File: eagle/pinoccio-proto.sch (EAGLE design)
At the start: 3 parts

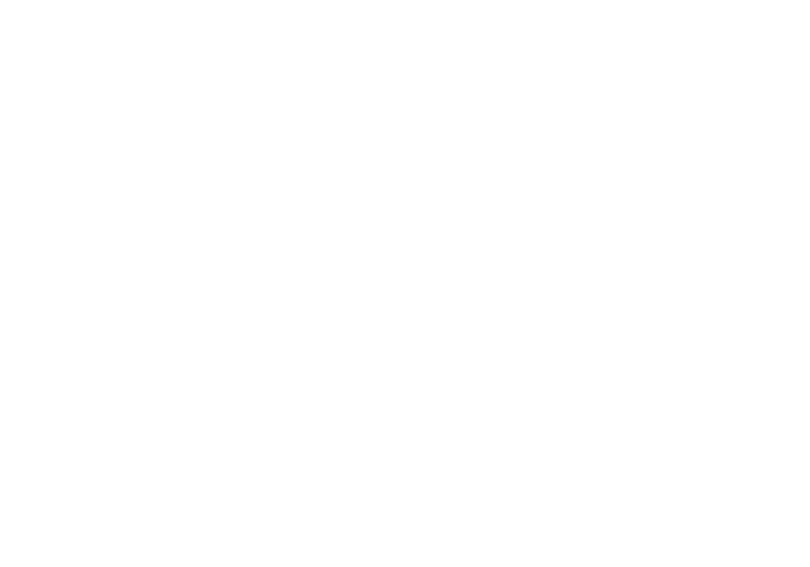
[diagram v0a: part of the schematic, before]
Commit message: Break out ground and power buses to pins
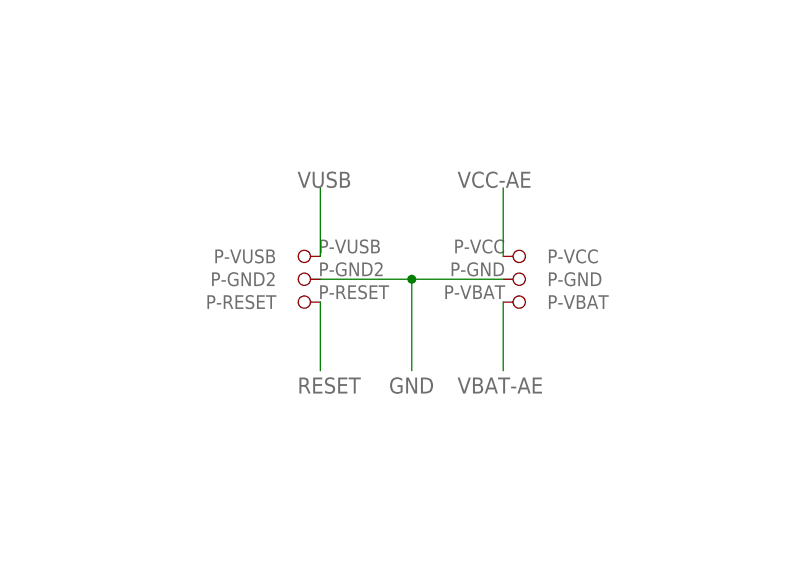
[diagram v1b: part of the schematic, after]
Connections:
- net GND: now also U$1.P$53, U$1.P$77, U$1.P-GND, U$1.P-GND2
- net RESET: now also U$1.P-RESET
- net VBAT-AE: now also U$1.P-VBAT
- net VCC-AE: now also U$1.P-VCC
- net VUSB: now also U$1.P-VUSB
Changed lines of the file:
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@@
 <label x="185.42" y="119.38" size="1.778" layer="95"/>
+</segment>
+<segment>
+<pinref part="U$1" gate="G$1" pin="P-GND"/>
+<pinref part="U$1" gate="G$1" pin="P-GND2"/>
+<wire x1="116.84" y1="127" x2="106.68" y2="127" width="0.1524" layer="91"/>
+<pinref part="U$1" gate="G$1" pin="P$77"/>
+<wire x1="96.52" y1="127" x2="106.68" y2="127" width="0.1524" layer="91"/>
+<pinref part="U$1" gate="G$1" pin="P$53"/>
+<wire x1="106.68" y1="127" x2="106.68" y2="116.84" width="0.1524" layer="91"/>
+<junction x="106.68" y="127"/>
+<label x="104.14" y="114.3" size="1.778" layer="95"/>
 </segment>
 </net>
@@
 <label x="185.42" y="175.26" size="1.778" layer="95"/>
 </segment>
+<segment>
+<pinref part="U$1" gate="G$1" pin="P-VUSB"/>
+<wire x1="96.52" y1="129.54" x2="96.52" y2="137.16" width="0.1524" layer="91"/>
+<label x="93.98" y="137.16" size="1.778" layer="95"/>
+</segment>
 </net>
 <net name="VBAT-AE" class="0">
@@
 <label x="185.42" y="116.84" size="1.778" layer="95"/>
 </segment>
+<segment>
+<pinref part="U$1" gate="G$1" pin="P-VBAT"/>
+<wire x1="116.84" y1="124.46" x2="116.84" y2="116.84" width="0.1524" layer="91"/>
+<label x="111.76" y="114.3" size="1.778" layer="95"/>
+</segment>
 </net>
 <net name="SSN" class="0">
@@
 <label x="185.42" y="170.18" size="1.778" layer="95"/>
 </segment>
+<segment>
+<pinref part="U$1" gate="G$1" pin="P-RESET"/>
+<wire x1="96.52" y1="124.46" x2="96.52" y2="116.84" width="0.1524" layer="91"/>
+<label x="93.98" y="114.3" size="1.778" layer="95"/>
+</segment>
 </net>
 <net name="A0" class="0">
@@
 <label x="185.42" y="121.92" size="1.778" layer="95"/>
 </segment>
-</net>
+<segment>
+<pinref part="U$1" gate="G$1" pin="P-VCC"/>
+<wire x1="116.84" y1="129.54" x2="116.84" y2="137.16" width="0.1524" layer="91"/>
+<label x="111.76" y="137.16" size="1.778" layer="95"/>
+</segment>
+</net>

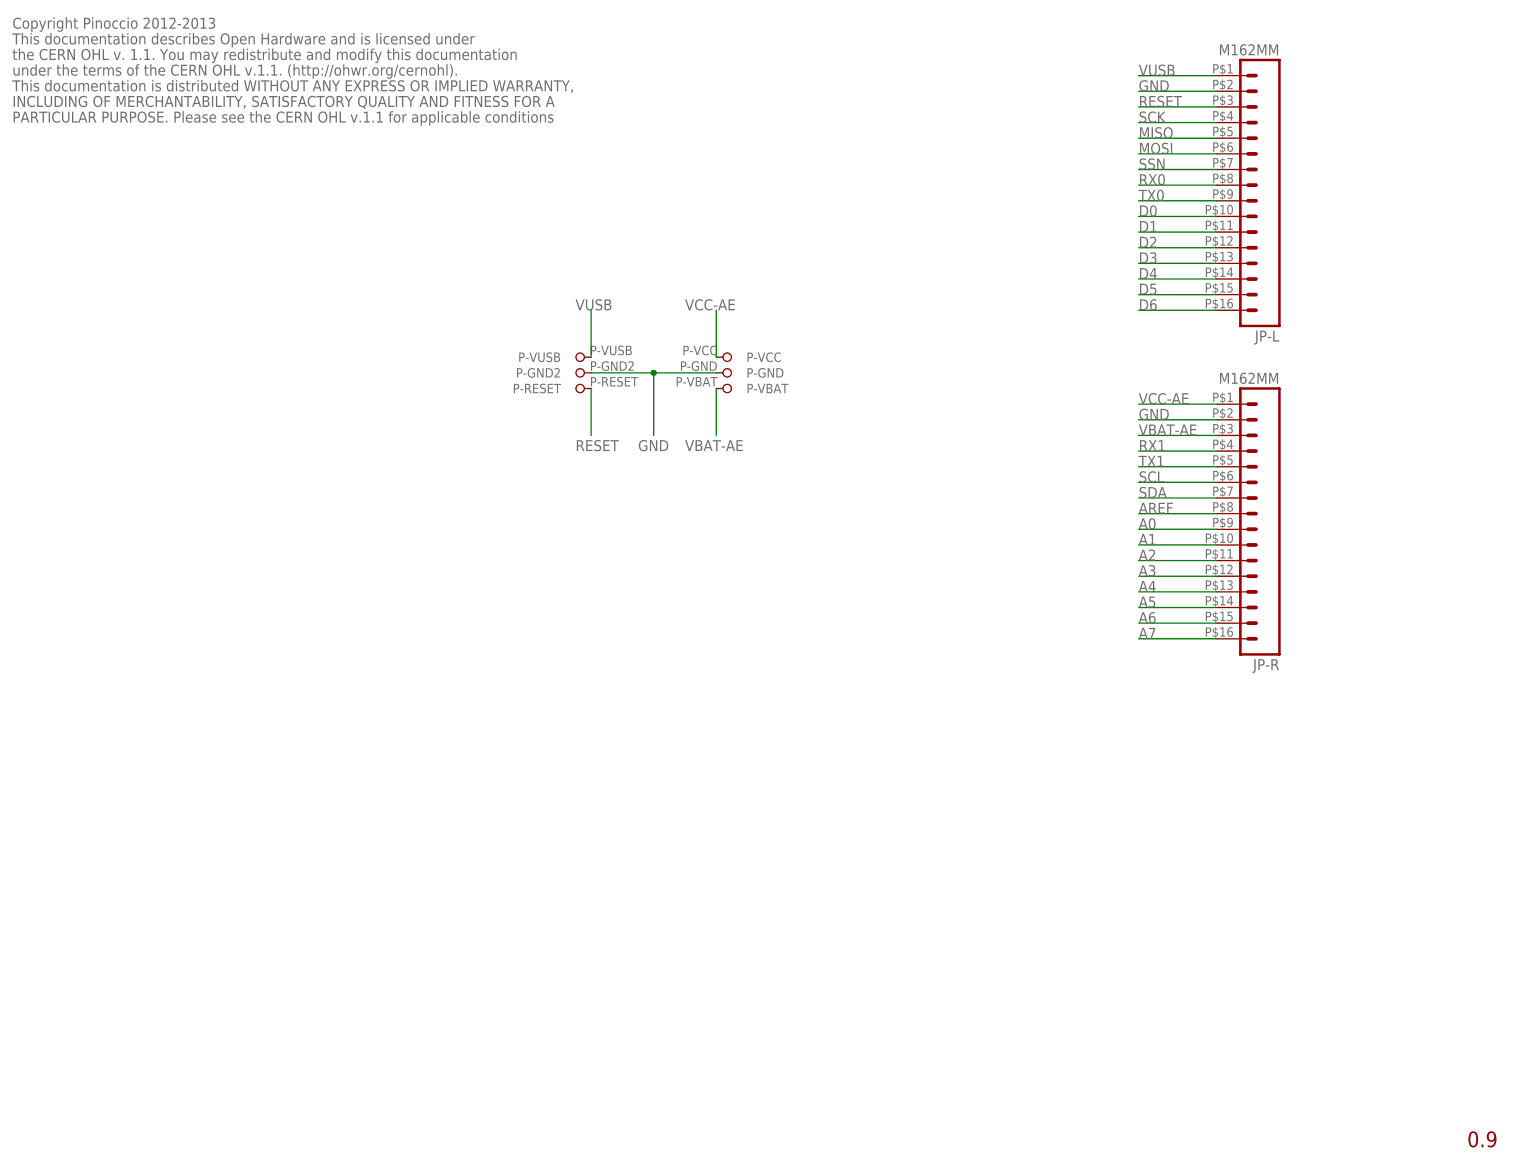
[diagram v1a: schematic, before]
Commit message: Update to v0.10, added solderable pads to bottom of board
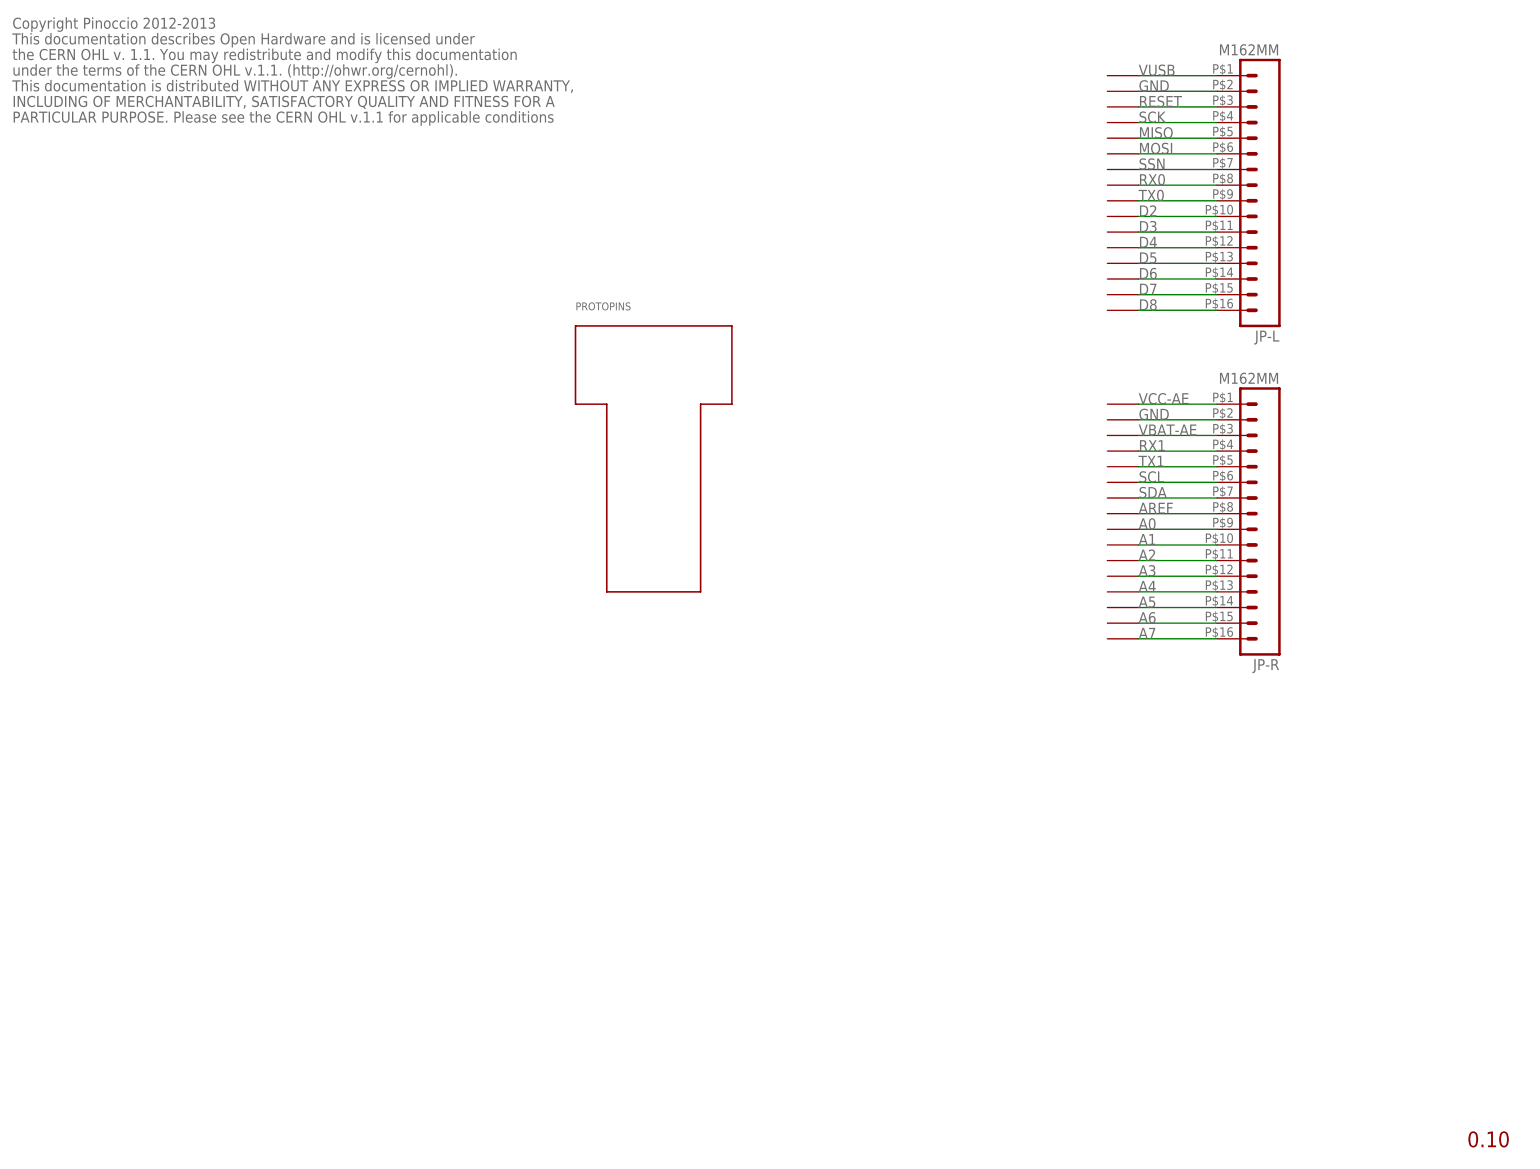
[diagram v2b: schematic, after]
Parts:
- added U$10, U$11, U$12, U$13, U$14, U$15, U$16, U$17, U$18, U$19, U$2, U$20, U$21, U$22, U$23, U$24, U$25, U$26, U$27, U$28, U$29, U$3, U$30, U$31, U$32, U$33, U$4, U$5, U$6, U$7, U$8, U$9: PAD55-RRECT, Pinoccio:PAD55-RRECT
- renumbered U$1 to PROTOPINS
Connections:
- removed net D0: JP-L.10
- removed net D1: JP-L.11
- new net D7: JP-L.15, U$2.P$1
- new net D8: JP-L.16, U$17.P$1
- net A0: now also U$25.P$1
- net A1: now also U$24.P$1
- net A2: now also U$23.P$1
- net A3: now also U$22.P$1
- net A4: now also U$21.P$1
- net A5: now also U$20.P$1
- net A6: now also U$19.P$1
- net A7: now also U$18.P$1
- net AREF: now also U$26.P$1
- net D2: now also JP-L.10, U$7.P$1; no longer JP-L.12
- net D3: now also JP-L.11, U$6.P$1; no longer JP-L.13
- net D4: now also JP-L.12, U$5.P$1; no longer JP-L.14
- net D5: now also JP-L.13, U$3.P$1; no longer JP-L.15
- net D6: now also JP-L.14, U$4.P$1; no longer JP-L.16
- net GND: now also U$15.P$1, U$32.P$1; no longer PROTOPINS.P$53, PROTOPINS.P$77, PROTOPINS.P-GND, PROTOPINS.P-GND2
- net MISO: now also U$12.P$1
- net MOSI: now also U$11.P$1
- net RESET: now also U$14.P$1; no longer PROTOPINS.P-RESET
- net RX0: now also U$9.P$1
- net RX1: now also U$30.P$1
- net SCK: now also U$13.P$1
- net SCL: now also U$28.P$1
- net SDA: now also U$27.P$1
- net SSN: now also U$10.P$1
- net TX0: now also U$8.P$1
- net TX1: now also U$29.P$1
- net VBAT-AE: now also U$31.P$1; no longer PROTOPINS.P-VBAT
- net VCC-AE: now also U$33.P$1; no longer PROTOPINS.P-VCC
- net VUSB: now also U$16.P$1; no longer PROTOPINS.P-VUSB
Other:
- note added: "0.10"
- note removed: "0.9"

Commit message: version 1.0
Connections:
- net VBAT-AE renamed VBAT
- new net BKPK-BUS: JP-L.2, U$15.P$1
- net GND: no longer JP-L.2, U$15.P$1
